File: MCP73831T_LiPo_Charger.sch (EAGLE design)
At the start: 8 parts, among them U4 MCP73831

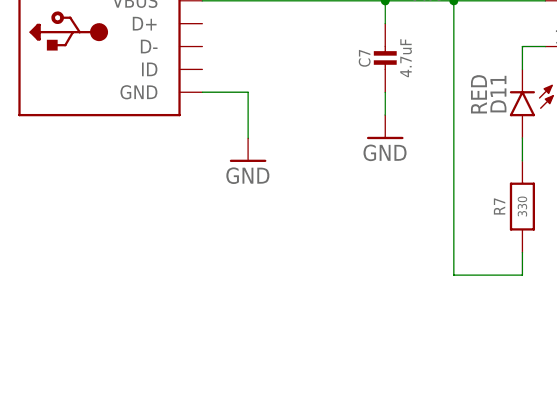
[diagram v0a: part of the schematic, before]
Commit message: added headers to schematic
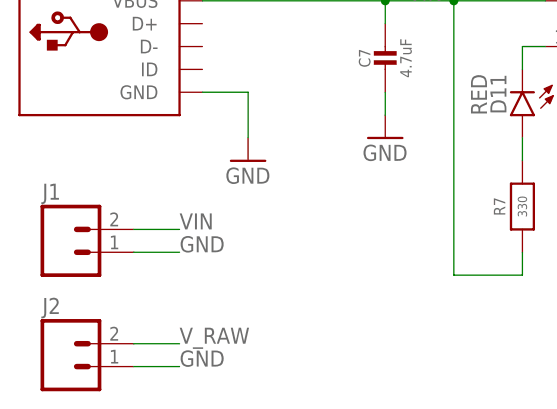
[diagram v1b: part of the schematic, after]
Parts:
- added J1, J2: (no value), SparkFun-Connectors:M02PTH
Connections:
- net GND: now also J1.1, J2.1
- net VIN: now also J1.2
- net V_RAW: now also J2.2
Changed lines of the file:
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@@
 <part name="GND1" library="SparkFun-Aesthetics" deviceset="GND" device=""/>
 <part name="X1" library="microbuilder" deviceset="USB" device="MICRO_20329"/>
+<part name="J1" library="SparkFun-Connectors" deviceset="M02" device="PTH"/>
+<part name="J2" library="SparkFun-Connectors" deviceset="M02" device="PTH"/>
 </parts>
 <sheets>
@@
 <instance part="GND1" gate="1" x="96.52" y="35.56"/>
 <instance part="X1" gate="G$1" x="20.32" y="63.5"/>
+<instance part="J1" gate="G$1" x="15.24" y="40.64"/>
+<instance part="J2" gate="G$1" x="15.24" y="27.94"/>
 </instances>
 <busses>
@@
 <pinref part="JP1" gate="G$1" pin="-"/>
 </segment>
+<segment>
+<pinref part="J1" gate="G$1" pin="1"/>
+<wire x1="22.86" y1="40.64" x2="27.94" y2="40.64" width="0.1524" layer="91"/>
+<label x="27.94" y="40.64" size="1.778" layer="95"/>
+</segment>
+<segment>
+<pinref part="J2" gate="G$1" pin="1"/>
+<wire x1="22.86" y1="27.94" x2="27.94" y2="27.94" width="0.1524" layer="91"/>
+<label x="27.94" y="27.94" size="1.778" layer="95"/>
+</segment>
 </net>
 <net name="V_RAW" class="0">
@@
 <pinref part="JP1" gate="G$1" pin="+"/>
 <pinref part="C8" gate="G$1" pin="1"/>
+</segment>
+<segment>
+<pinref part="J2" gate="G$1" pin="2"/>
+<wire x1="22.86" y1="30.48" x2="27.94" y2="30.48" width="0.1524" layer="91"/>
+<label x="27.94" y="30.48" size="1.778" layer="95"/>
 </segment>
 </net>
@@
 <junction x="50.8" y="68.58"/>
 </segment>
+<segment>
+<pinref part="J1" gate="G$1" pin="2"/>
+<wire x1="22.86" y1="43.18" x2="27.94" y2="43.18" width="0.1524" layer="91"/>
+<label x="27.94" y="43.18" size="1.778" layer="95"/>
+</segment>
 </net>

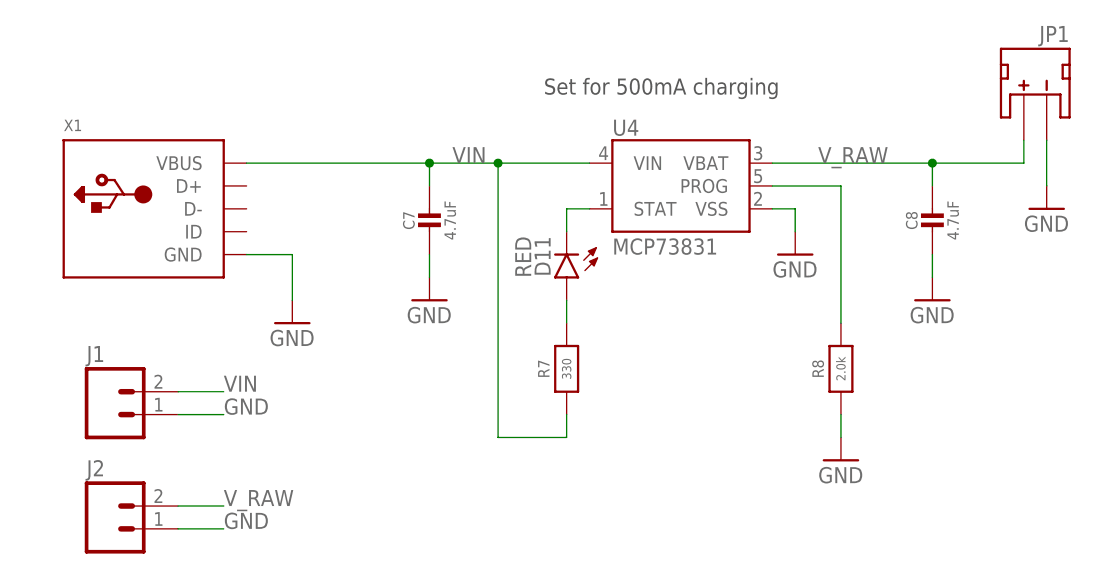
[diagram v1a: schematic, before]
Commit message: modified microUSB port
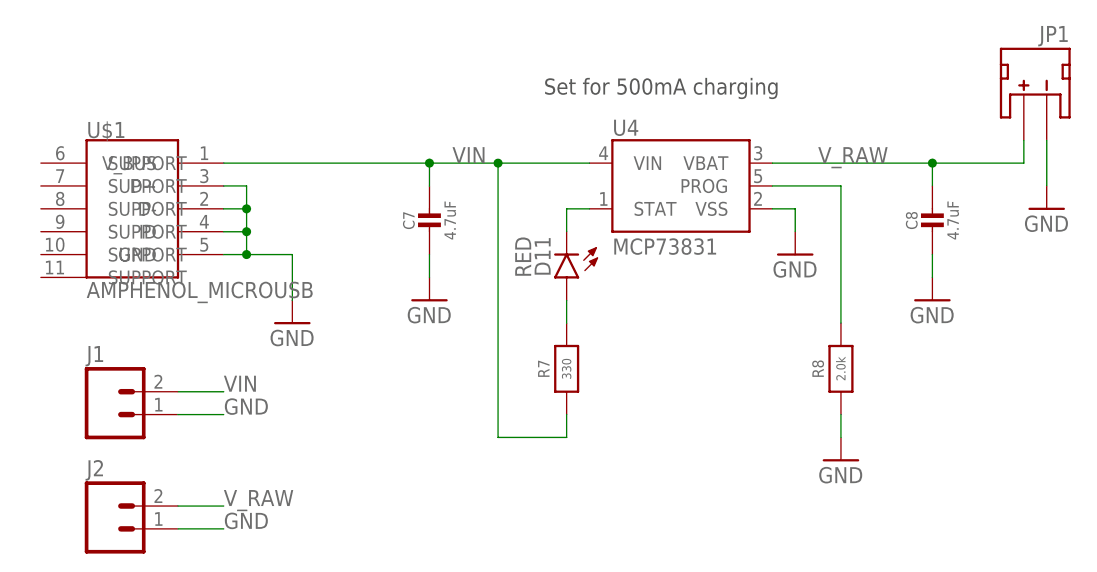
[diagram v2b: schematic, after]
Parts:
- removed X1: (no value), microbuilder:USBMICRO_20329
- added U$1: AMPHENOL_MICROUSB, sharkdunio:AMPHENOL_MICROUSB
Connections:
- net GND: now also U$1.D+, U$1.D-, U$1.GND, U$1.ID; no longer X1.GND
- net VIN: now also U$1.V_BUS; no longer X1.VBUS
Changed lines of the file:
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@@
 <part name="C8" library="microbuilder" deviceset="CAP_CERAMIC" device="0805-NOOUTLINE" value="4.7uF"/>
 <part name="GND1" library="SparkFun-Aesthetics" deviceset="GND" device=""/>
-<part name="X1" library="microbuilder" deviceset="USB" device="MICRO_20329"/>
 <part name="J1" library="SparkFun-Connectors" deviceset="M02" device="PTH"/>
 <part name="J2" library="SparkFun-Connectors" deviceset="M02" device="PTH"/>
+<part name="U$1" library="sharkdunio" deviceset="AMPHENOL_MICROUSB" device=""/>
 </parts>
 <sheets>
@@
 <instance part="C8" gate="G$1" x="106.68" y="60.96"/>
 <instance part="GND1" gate="1" x="96.52" y="35.56"/>
-<instance part="X1" gate="G$1" x="20.32" y="63.5"/>
 <instance part="J1" gate="G$1" x="15.24" y="40.64"/>
 <instance part="J2" gate="G$1" x="15.24" y="27.94"/>
+<instance part="U$1" gate="G$1" x="17.78" y="60.96"/>
 </instances>
 <busses>
@@
 <pinref part="GND15" gate="1" pin="GND"/>
 <wire x1="35.56" y1="53.34" x2="35.56" y2="58.42" width="0.1524" layer="91"/>
-<pinref part="X1" gate="G$1" pin="GND"/>
+<wire x1="27.94" y1="58.42" x2="30.48" y2="58.42" width="0.1524" layer="91"/>
+<pinref part="U$1" gate="G$1" pin="GND"/>
+<pinref part="U$1" gate="G$1" pin="ID"/>
 <wire x1="30.48" y1="58.42" x2="35.56" y2="58.42" width="0.1524" layer="91"/>
+<wire x1="27.94" y1="60.96" x2="30.48" y2="60.96" width="0.1524" layer="91"/>
+<wire x1="30.48" y1="60.96" x2="30.48" y2="58.42" width="0.1524" layer="91"/>
+<junction x="30.48" y="58.42"/>
+<pinref part="U$1" gate="G$1" pin="D-"/>
+<wire x1="27.94" y1="63.5" x2="30.48" y2="63.5" width="0.1524" layer="91"/>
+<wire x1="30.48" y1="63.5" x2="30.48" y2="60.96" width="0.1524" layer="91"/>
+<junction x="30.48" y="60.96"/>
+<pinref part="U$1" gate="G$1" pin="D+"/>
+<wire x1="27.94" y1="66.04" x2="30.48" y2="66.04" width="0.1524" layer="91"/>
+<wire x1="30.48" y1="66.04" x2="30.48" y2="63.5" width="0.1524" layer="91"/>
+<junction x="30.48" y="63.5"/>
 </segment>
 <segment>
@@
 <pinref part="R7" gate="G$1" pin="1"/>
 <pinref part="C7" gate="G$1" pin="1"/>
-<pinref part="X1" gate="G$1" pin="VBUS"/>
-<wire x1="30.48" y1="68.58" x2="50.8" y2="68.58" width="0.1524" layer="91"/>
+<wire x1="27.94" y1="68.58" x2="50.8" y2="68.58" width="0.1524" layer="91"/>
 <junction x="50.8" y="68.58"/>
+<pinref part="U$1" gate="G$1" pin="V_BUS"/>
 </segment>
 <segment>

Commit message: modified microusb port and lipo schematic
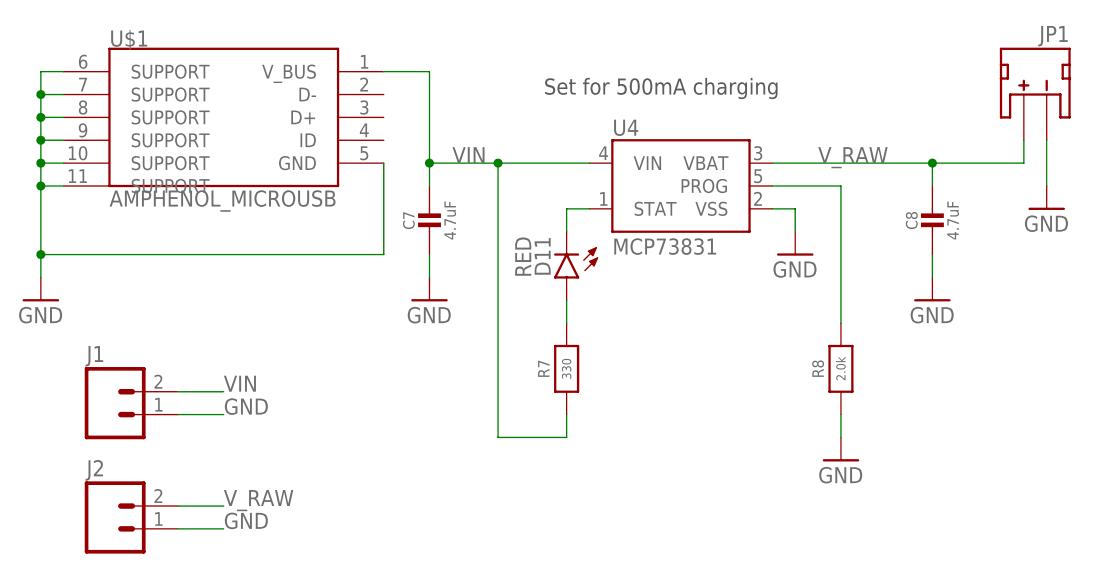
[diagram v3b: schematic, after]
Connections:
- net GND: now also U$1.SUPPORT@1, U$1.SUPPORT@2, U$1.SUPPORT@3, U$1.SUPPORT@4, U$1.SUPPORT@5, U$1.SUPPORT@6; no longer U$1.D+, U$1.D-, U$1.ID
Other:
- moved on the sheet: U$1
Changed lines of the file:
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@@
 <instance part="GND4" gate="1" x="119.38" y="63.5"/>
 <instance part="D11" gate="G$1" x="66.04" y="55.88" rot="R180"/>
-<instance part="GND15" gate="1" x="35.56" y="50.8"/>
+<instance part="GND15" gate="1" x="7.62" y="53.34"/>
 <instance part="GND14" gate="1" x="106.68" y="53.34"/>
 <instance part="GND17" gate="1" x="50.8" y="53.34"/>
@@
 <instance part="J1" gate="G$1" x="15.24" y="40.64"/>
 <instance part="J2" gate="G$1" x="15.24" y="27.94"/>
-<instance part="U$1" gate="G$1" x="17.78" y="60.96"/>
+<instance part="U$1" gate="G$1" x="20.32" y="71.12"/>
 </instances>
 <busses>
@@
 <segment>
 <pinref part="GND15" gate="1" pin="GND"/>
-<wire x1="35.56" y1="53.34" x2="35.56" y2="58.42" width="0.1524" layer="91"/>
-<wire x1="27.94" y1="58.42" x2="30.48" y2="58.42" width="0.1524" layer="91"/>
+<pinref part="U$1" gate="G$1" pin="SUPPORT@1"/>
+<wire x1="10.16" y1="78.74" x2="7.62" y2="78.74" width="0.1524" layer="91"/>
+<wire x1="7.62" y1="78.74" x2="7.62" y2="76.2" width="0.1524" layer="91"/>
+<pinref part="U$1" gate="G$1" pin="SUPPORT@2"/>
+<wire x1="7.62" y1="76.2" x2="7.62" y2="73.66" width="0.1524" layer="91"/>
+<wire x1="7.62" y1="73.66" x2="7.62" y2="71.12" width="0.1524" layer="91"/>
+<wire x1="7.62" y1="71.12" x2="7.62" y2="68.58" width="0.1524" layer="91"/>
+<wire x1="7.62" y1="68.58" x2="7.62" y2="66.04" width="0.1524" layer="91"/>
+<wire x1="7.62" y1="66.04" x2="7.62" y2="58.42" width="0.1524" layer="91"/>
+<wire x1="7.62" y1="58.42" x2="7.62" y2="55.88" width="0.1524" layer="91"/>
+<wire x1="10.16" y1="76.2" x2="7.62" y2="76.2" width="0.1524" layer="91"/>
+<junction x="7.62" y="76.2"/>
+<pinref part="U$1" gate="G$1" pin="SUPPORT@3"/>
+<wire x1="10.16" y1="73.66" x2="7.62" y2="73.66" width="0.1524" layer="91"/>
+<junction x="7.62" y="73.66"/>
+<pinref part="U$1" gate="G$1" pin="SUPPORT@4"/>
+<wire x1="10.16" y1="71.12" x2="7.62" y2="71.12" width="0.1524" layer="91"/>
+<junction x="7.62" y="71.12"/>
+<pinref part="U$1" gate="G$1" pin="SUPPORT@5"/>
+<wire x1="10.16" y1="68.58" x2="7.62" y2="68.58" width="0.1524" layer="91"/>
+<junction x="7.62" y="68.58"/>
+<pinref part="U$1" gate="G$1" pin="SUPPORT@6"/>
+<wire x1="10.16" y1="66.04" x2="7.62" y2="66.04" width="0.1524" layer="91"/>
+<junction x="7.62" y="66.04"/>
 <pinref part="U$1" gate="G$1" pin="GND"/>
-<pinref part="U$1" gate="G$1" pin="ID"/>
-<wire x1="30.48" y1="58.42" x2="35.56" y2="58.42" width="0.1524" layer="91"/>
-<wire x1="27.94" y1="60.96" x2="30.48" y2="60.96" width="0.1524" layer="91"/>
-<wire x1="30.48" y1="60.96" x2="30.48" y2="58.42" width="0.1524" layer="91"/>
-<junction x="30.48" y="58.42"/>
-<pinref part="U$1" gate="G$1" pin="D-"/>
-<wire x1="27.94" y1="63.5" x2="30.48" y2="63.5" width="0.1524" layer="91"/>
-<wire x1="30.48" y1="63.5" x2="30.48" y2="60.96" width="0.1524" layer="91"/>
-<junction x="30.48" y="60.96"/>
-<pinref part="U$1" gate="G$1" pin="D+"/>
-<wire x1="27.94" y1="66.04" x2="30.48" y2="66.04" width="0.1524" layer="91"/>
-<wire x1="30.48" y1="66.04" x2="30.48" y2="63.5" width="0.1524" layer="91"/>
-<junction x="30.48" y="63.5"/>
+<wire x1="45.72" y1="68.58" x2="45.72" y2="58.42" width="0.1524" layer="91"/>
+<wire x1="45.72" y1="58.42" x2="7.62" y2="58.42" width="0.1524" layer="91"/>
+<junction x="7.62" y="58.42"/>
 </segment>
 <segment>
@@
 <pinref part="R7" gate="G$1" pin="1"/>
 <pinref part="C7" gate="G$1" pin="1"/>
-<wire x1="27.94" y1="68.58" x2="50.8" y2="68.58" width="0.1524" layer="91"/>
+<pinref part="U$1" gate="G$1" pin="V_BUS"/>
+<wire x1="45.72" y1="78.74" x2="50.8" y2="78.74" width="0.1524" layer="91"/>
+<wire x1="50.8" y1="78.74" x2="50.8" y2="68.58" width="0.1524" layer="91"/>
 <junction x="50.8" y="68.58"/>
-<pinref part="U$1" gate="G$1" pin="V_BUS"/>
 </segment>
 <segment>
